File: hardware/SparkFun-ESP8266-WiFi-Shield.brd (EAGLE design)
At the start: 59.7 x 53.3 mm, 62 parts, among them Q1 BSS138, Q2 BSS138, U1 AP2112K-3.3V, U2 ESP8266, U3 AT25SF041-SOIC8, Y1 26MHz

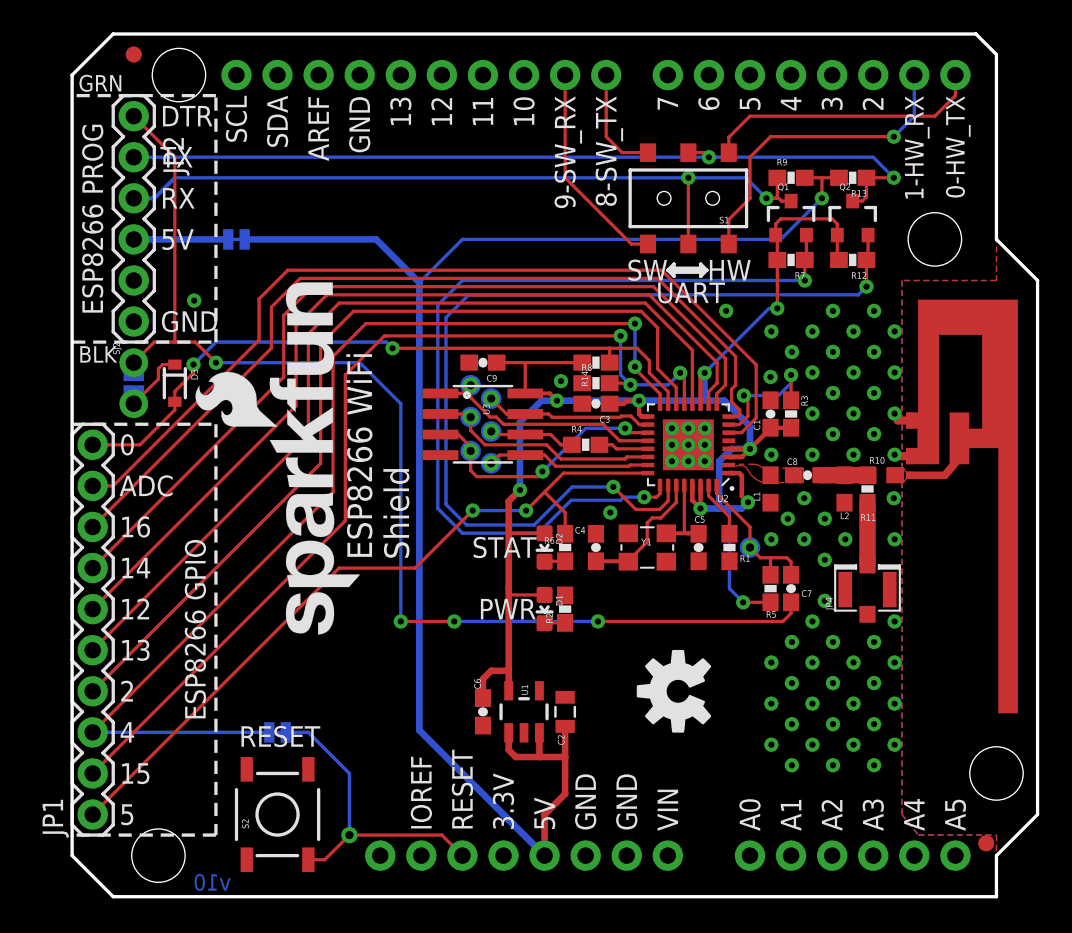
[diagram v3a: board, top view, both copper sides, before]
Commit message: Breaking out ESP8266 reset pin.
Moved the FTDI header to avoid interfering with screw head.
Moved position of GPIO5 break out.
Renamed GPIO16 to XPD.
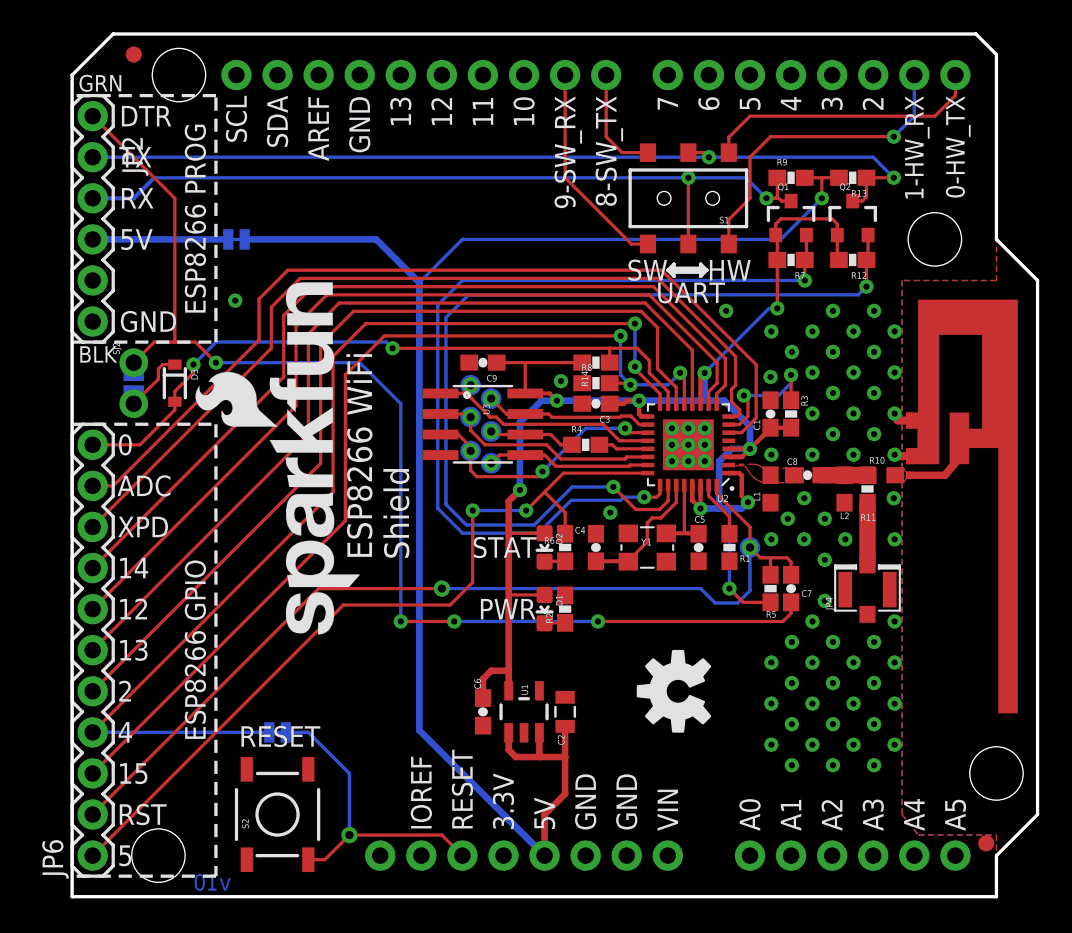
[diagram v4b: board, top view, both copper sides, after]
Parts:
- removed JP1: M10SILK_FEMALE_PTH, SparkFun-Connectors:1X10
- added JP6: (no value), SparkFun-Connectors:1X11
- moved JP2 2.54 mm to (1.27, 48.3)
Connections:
- removed net GPIO14/SCL: JP1.7, U2.9
- removed net GPIO16: JP1.8, U2.8
- removed net GPIO2/SDA: JP1.4, U2.14
- new net GPIO14: JP6.8, U2.9
- new net GPIO2: JP6.5, U2.14
- new net XPD: JP6.9, U2.8
- net ADC: now also JP6.10; no longer JP1.9
- net GPIO0: now also JP6.11; no longer JP1.10
- net GPIO12: now also JP6.7; no longer JP1.6
- net GPIO13: now also JP6.6; no longer JP1.5
- net GPIO15: now also JP6.3; no longer JP1.2
- net GPIO4: now also JP6.4; no longer JP1.3
- net GPIO5: now also JP6.1; no longer JP1.1
- net RESET: now also JP6.2
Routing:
- net GPIO2/SDA: track 54.6 -> 0.00 mm
- net GPIO2: track 0.00 -> 54.6 mm
- net XPD: track 0.00 -> 54.2 mm
- net GPIO16: track 54.2 -> 0.00 mm
- net GPIO14/SCL: track 53.5 -> 0.00 mm
- net GPIO14: track 0.00 -> 53.5 mm
- net RESET: track 9.47 -> 59.2 mm, vias 1 -> 2
- net GPIO5: track 46.2 -> 49.8 mm
- net N$7: track 5.84 -> 8.38 mm
- net TX_HIGH: track 52.7 -> 55.3 mm
- net RX_HIGH: track 47.8 -> 50.3 mm
- net DTR: track 72.9 -> 74.0 mm
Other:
- outline, holes or cut-outs redrawn
- board text added: "XPD"
- board text removed: "16"

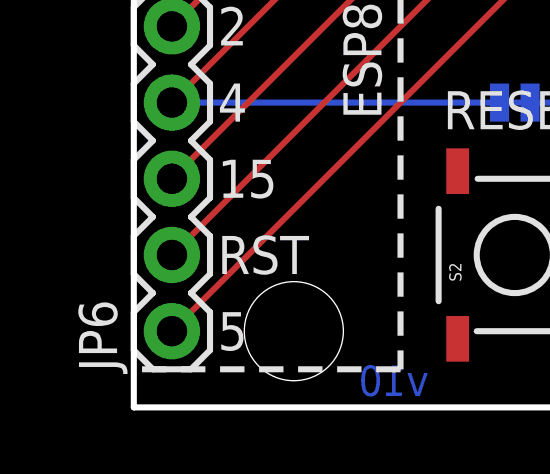
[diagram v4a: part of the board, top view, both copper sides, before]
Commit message: Cleaning up schematic.
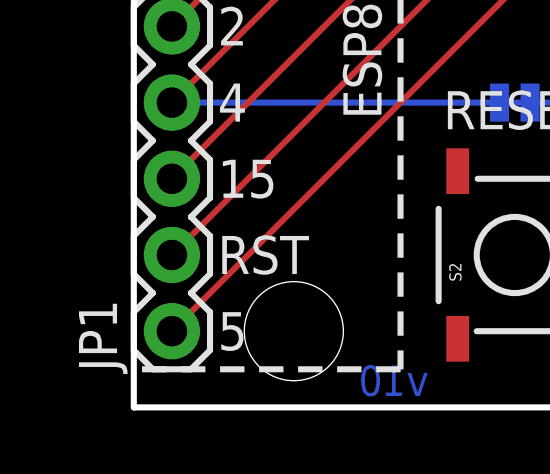
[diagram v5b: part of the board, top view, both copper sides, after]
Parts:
- renumbered JP6 to JP1
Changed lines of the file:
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@@
 <element name="SJ1" library="SparkFun-Passives" package="PAD-JUMPER-2-NO_NO_SILK" value="" x="3.81" y="31.75" rot="MR270"/>
 <element name="SJ2" library="SparkFun-Passives" package="PTH-JUMPER-2-NO_NO_SILK" value="" x="3.81" y="31.75" rot="R270"/>
-<element name="JP6" library="SparkFun-Connectors" package="1X11" value="" x="1.27" y="2.54" rot="R90"/>
+<element name="JP1" library="SparkFun-Connectors" package="1X11" value="" x="1.27" y="2.54" rot="R90"/>
 </elements>
 <signals>
@@
 <wire x1="41.91" y1="21.59" x2="41.91" y2="18.923" width="0.2032" layer="16"/>
 <wire x1="42.545" y1="20.955" x2="41.91" y2="21.59" width="0.2032" layer="1"/>
-<contactref element="JP6" pad="2"/>
+<contactref element="JP1" pad="2"/>
 <wire x1="1.27" y1="5.08" x2="15.24" y2="19.05" width="0.2032" layer="1"/>
 </signal>
@@
 <wire x1="13.081" y1="32.131" x2="13.081" y2="35.941" width="0.2032" layer="1"/>
 <wire x1="13.081" y1="35.941" x2="14.859" y2="37.719" width="0.2032" layer="1"/>
-<contactref element="JP6" pad="8"/>
+<contactref element="JP1" pad="8"/>
 </signal>
 <signal name="ADC">
@@
 <wire x1="11.557" y1="34.417" x2="11.557" y2="36.957" width="0.2032" layer="1"/>
 <wire x1="11.557" y1="36.957" x2="13.335" y2="38.735" width="0.2032" layer="1"/>
-<contactref element="JP6" pad="10"/>
+<contactref element="JP1" pad="10"/>
 </signal>
 <signal name="GPIO0">
@@
 <wire x1="6.35" y1="31.242" x2="7.5" y2="32.392" width="0.2032" layer="1"/>
 <wire x1="7.5" y1="32.392" x2="7.5" y2="32.9" width="0.2032" layer="1"/>
-<contactref element="JP6" pad="11"/>
+<contactref element="JP1" pad="11"/>
 </signal>
 <signal name="GPIO5">
@@
 <wire x1="30.48" y1="22.44" x2="30.48" y2="23.749" width="0.2032" layer="1"/>
 <wire x1="30.48" y1="23.749" x2="29.21" y2="25.019" width="0.2032" layer="1"/>
-<contactref element="JP6" pad="1"/>
+<contactref element="JP1" pad="1"/>
 <wire x1="24.765" y1="23.876" x2="24.765" y2="19.431" width="0.2032" layer="1"/>
 <wire x1="24.765" y1="19.431" x2="23.368" y2="18.034" width="0.2032" layer="1"/>
@@
 <contactref element="SJ4" pad="2"/>
 <wire x1="1.27" y1="10.16" x2="12.192" y2="10.16" width="0.2032" layer="16"/>
-<contactref element="JP6" pad="4"/>
+<contactref element="JP1" pad="4"/>
 </signal>
 <signal name="SD_!WP!">
@@
 <wire x1="12.319" y1="33.909" x2="12.319" y2="36.449" width="0.2032" layer="1"/>
 <wire x1="12.319" y1="36.449" x2="14.097" y2="38.227" width="0.2032" layer="1"/>
-<contactref element="JP6" pad="9"/>
+<contactref element="JP1" pad="9"/>
 </signal>
 <signal name="GPIO15">
@@
 <wire x1="16.891" y1="23.241" x2="16.891" y2="32.258" width="0.2032" layer="1"/>
 <wire x1="16.891" y1="32.258" x2="19.304" y2="34.671" width="0.2032" layer="1"/>
-<contactref element="JP6" pad="3"/>
+<contactref element="JP1" pad="3"/>
 </signal>
 <signal name="GPIO13">
@@
 <wire x1="14.605" y1="28.575" x2="14.605" y2="34.798" width="0.2032" layer="1"/>
 <wire x1="14.605" y1="34.798" x2="16.51" y2="36.703" width="0.2032" layer="1"/>
-<contactref element="JP6" pad="6"/>
+<contactref element="JP1" pad="6"/>
 </signal>
 <signal name="GPIO12">
@@
 <wire x1="13.843" y1="30.353" x2="13.843" y2="35.306" width="0.2032" layer="1"/>
 <wire x1="13.843" y1="35.306" x2="15.748" y2="37.211" width="0.2032" layer="1"/>
-<contactref element="JP6" pad="7"/>
+<contactref element="JP1" pad="7"/>
 </signal>
 <signal name="GPIO2">
@@
 <wire x1="15.367" y1="26.797" x2="15.367" y2="34.163" width="0.2032" layer="1"/>
 <wire x1="15.367" y1="34.163" x2="17.399" y2="36.195" width="0.2032" layer="1"/>
-<contactref element="JP6" pad="5"/>
+<contactref element="JP1" pad="5"/>
 </signal>
 <signal name="N$6">

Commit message: Minor mods after running checklist.
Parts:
- SJ4: device SparkFun-Passives:PAD-JUMPER-2-NC_BY_TRACE_YES_SILK -> SparkFun-Passives:PAD-JUMPER-2-NO_YES_SILK
- moved LOGO3 1.80 mm to (32.4, 18.7)
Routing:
- net GPIO15: track 59.2 -> 59.9 mm
- net DTR: track 74.0 -> 74.7 mm
- net 5V: track 100.3 -> 100.8 mm
- net RESET: vias 2 -> 4
- net GND: vias 73 -> 77

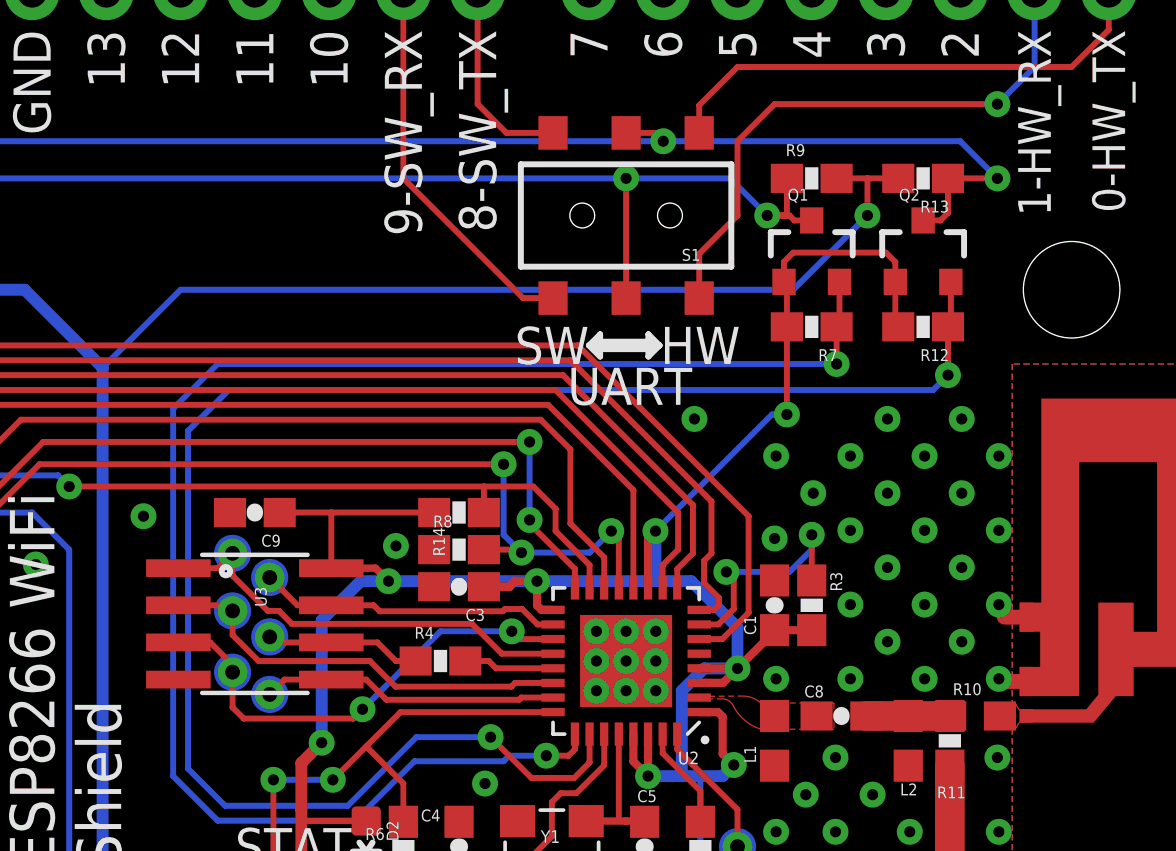
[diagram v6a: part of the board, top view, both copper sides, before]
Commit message: Small re-routes to increase ground plane coverage.
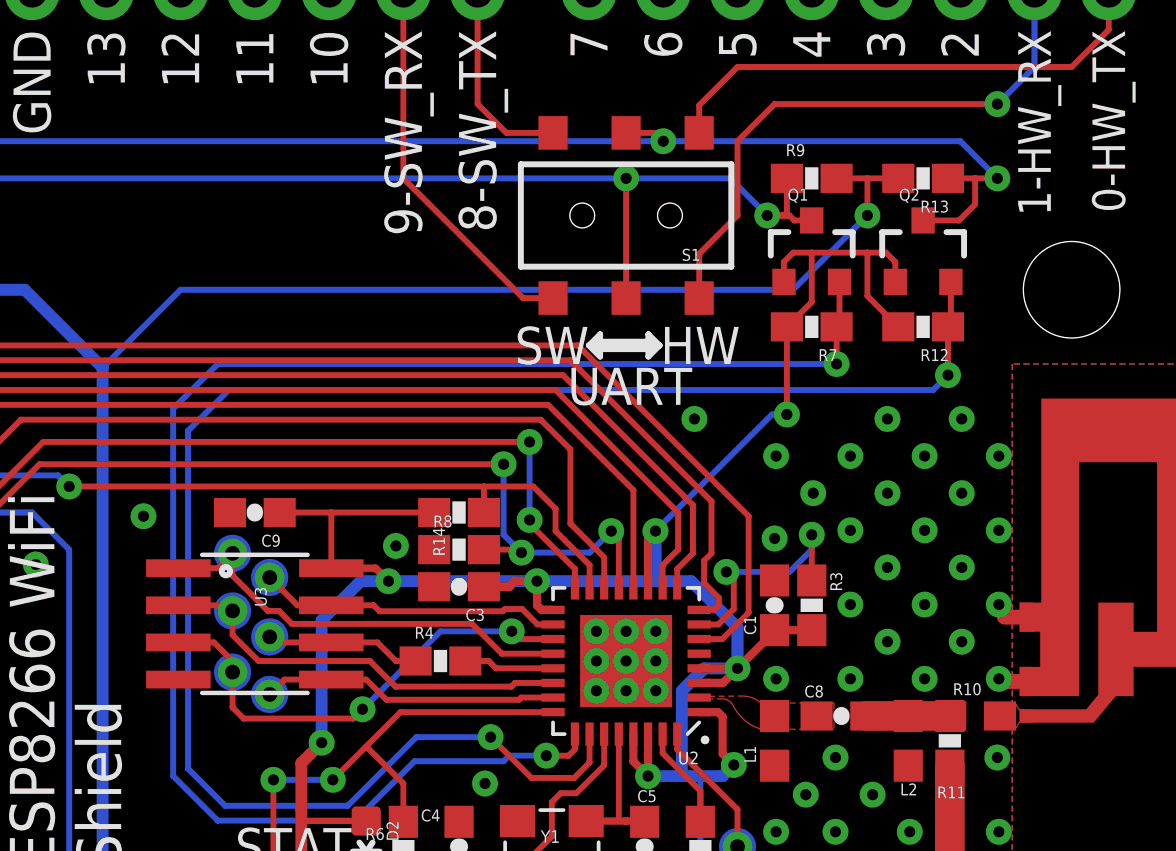
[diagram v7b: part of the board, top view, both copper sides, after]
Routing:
- net VCC: track 105.2 -> 108.0 mm
- net TX_HIGH: track 55.3 -> 56.0 mm
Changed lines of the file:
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@@
 <layer number="14" name="Route14" color="1" fill="6" visible="no" active="no"/>
 <layer number="15" name="Route15" color="4" fill="6" visible="no" active="no"/>
-<layer number="16" name="Bottom" color="1" fill="1" visible="yes" active="yes"/>
+<layer number="16" name="Bottom" color="1" fill="1" visible="no" active="yes"/>
 <layer number="17" name="Pads" color="2" fill="1" visible="yes" active="yes"/>
 <layer number="18" name="Vias" color="2" fill="1" visible="yes" active="yes"/>
-<layer number="19" name="Unrouted" color="6" fill="1" visible="yes" active="yes"/>
+<layer number="19" name="Unrouted" color="6" fill="1" visible="no" active="yes"/>
 <layer number="20" name="Dimension" color="15" fill="1" visible="yes" active="yes"/>
 <layer number="21" name="tPlace" color="16" fill="1" visible="yes" active="yes"/>
-<layer number="22" name="bPlace" color="14" fill="1" visible="yes" active="yes"/>
+<layer number="22" name="bPlace" color="14" fill="1" visible="no" active="yes"/>
 <layer number="23" name="tOrigins" color="15" fill="1" visible="yes" active="yes"/>
-<layer number="24" name="bOrigins" color="15" fill="1" visible="yes" active="yes"/>
+<layer number="24" name="bOrigins" color="15" fill="1" visible="no" active="yes"/>
 <layer number="25" name="tNames" color="7" fill="1" visible="no" active="yes"/>
 <layer number="26" name="bNames" color="7" fill="1" visible="no" active="yes"/>
@@
 <layer number="47" name="Measures" color="7" fill="1" visible="no" active="yes"/>
 <layer number="48" name="Document" color="7" fill="1" visible="no" active="yes"/>
-<layer number="49" name="Reference" color="7" fill="1" visible="yes" active="yes"/>
+<layer number="49" name="Reference" color="7" fill="1" visible="no" active="yes"/>
 <layer number="50" name="dxf" color="7" fill="1" visible="no" active="no"/>
 <layer number="51" name="tDocu" color="6" fill="1" visible="yes" active="yes"/>
@@
 <wire x1="26.99" y1="22.86" x2="26.99" y2="24.45" width="0.4064" layer="1"/>
 <wire x1="26.99" y1="24.45" x2="27.686" y2="25.146" width="0.4064" layer="1"/>
-<wire x1="47.41" y1="39.37" x2="47.31" y2="39.47" width="0.2032" layer="1"/>
-<wire x1="47.31" y1="39.47" x2="47.31" y2="40.91" width="0.2032" layer="1"/>
 <wire x1="43.5" y1="40.91" x2="43.5" y2="41.595" width="0.2032" layer="1"/>
 <wire x1="43.5" y1="41.595" x2="43.815" y2="41.91" width="0.2032" layer="1"/>
-<wire x1="43.815" y1="41.91" x2="46.99" y2="41.91" width="0.2032" layer="1"/>
+<wire x1="43.815" y1="41.91" x2="44.45" y2="41.91" width="0.2032" layer="1"/>
+<wire x1="44.45" y1="41.91" x2="46.355" y2="41.91" width="0.2032" layer="1"/>
+<wire x1="46.355" y1="41.91" x2="46.99" y2="41.91" width="0.2032" layer="1"/>
 <wire x1="46.99" y1="41.91" x2="47.31" y2="41.59" width="0.2032" layer="1"/>
 <wire x1="47.31" y1="40.91" x2="47.31" y2="41.59" width="0.2032" layer="1"/>
-<wire x1="43.6" y1="39.37" x2="43.6" y2="40.81" width="0.2032" layer="1"/>
 <wire x1="43.6" y1="40.81" x2="43.5" y2="40.91" width="0.2032" layer="1"/>
 <wire x1="29.21" y1="18.657" x2="26.99" y2="18.657" width="0.2032" layer="1"/>
@@
 <via x="40.64" y="19.05" extent="1-16" drill="0.381"/>
 <wire x1="40.64" y1="19.05" x2="41.49" y2="18.2" width="0.2032" layer="1"/>
+<wire x1="43.6" y1="39.37" x2="44.45" y2="40.22" width="0.2032" layer="1"/>
+<wire x1="44.45" y1="40.22" x2="44.45" y2="41.91" width="0.2032" layer="1"/>
+<wire x1="47.41" y1="39.37" x2="46.355" y2="40.425" width="0.2032" layer="1"/>
+<wire x1="46.355" y1="40.425" x2="46.355" y2="41.91" width="0.2032" layer="1"/>
 </signal>
 <signal name="GND">
@@
 <wire x1="25.019" y1="25.9715" x2="24.638" y2="26.3525" width="0.2032" layer="1"/>
 <wire x1="24.638" y1="26.3525" x2="24.638" y2="27.559" width="0.2032" layer="1"/>
-<wire x1="22.7838" y1="28.575" x2="23.876" y2="28.575" width="0.2032" layer="1"/>
-<wire x1="23.876" y1="28.575" x2="24.638" y2="27.813" width="0.2032" layer="1"/>
-<wire x1="24.638" y1="27.813" x2="24.638" y2="27.559" width="0.2032" layer="1"/>
+<wire x1="22.7838" y1="28.575" x2="24.003" y2="28.575" width="0.2032" layer="1"/>
+<wire x1="24.003" y1="28.575" x2="24.638" y2="27.94" width="0.2032" layer="1"/>
+<wire x1="24.638" y1="27.94" x2="24.638" y2="27.559" width="0.2032" layer="1"/>
 <contactref element="TP1" pad="P$1"/>
 </signal>
@@
 <wire x1="39.085" y1="46.005" x2="39.37" y2="45.72" width="0.2032" layer="1"/>
 <via x="39.37" y="45.72" extent="1-16" drill="0.381"/>
-<wire x1="49.11" y1="44.45" x2="50.8" y2="44.45" width="0.2032" layer="1"/>
-<wire x1="48.26" y1="43.01" x2="48.852" y2="43.01" width="0.2032" layer="1"/>
-<wire x1="48.852" y1="43.01" x2="49.11" y2="43.268" width="0.2032" layer="1"/>
-<wire x1="49.11" y1="44.45" x2="49.11" y2="43.268" width="0.2032" layer="1"/>
+<wire x1="49.11" y1="44.45" x2="50.038" y2="44.45" width="0.2032" layer="1"/>
+<wire x1="50.038" y1="44.45" x2="50.8" y2="44.45" width="0.2032" layer="1"/>
+<wire x1="48.26" y1="43.01" x2="49.487" y2="43.01" width="0.2032" layer="1"/>
+<wire x1="49.487" y1="43.01" x2="50.038" y2="43.561" width="0.2032" layer="1"/>
+<wire x1="50.038" y1="43.561" x2="50.038" y2="44.45" width="0.2032" layer="1"/>
 </signal>
 <signal name="5V">
